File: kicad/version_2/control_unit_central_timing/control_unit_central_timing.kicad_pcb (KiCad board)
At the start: 2 copper layers, 100 x 100 mm, 25 parts

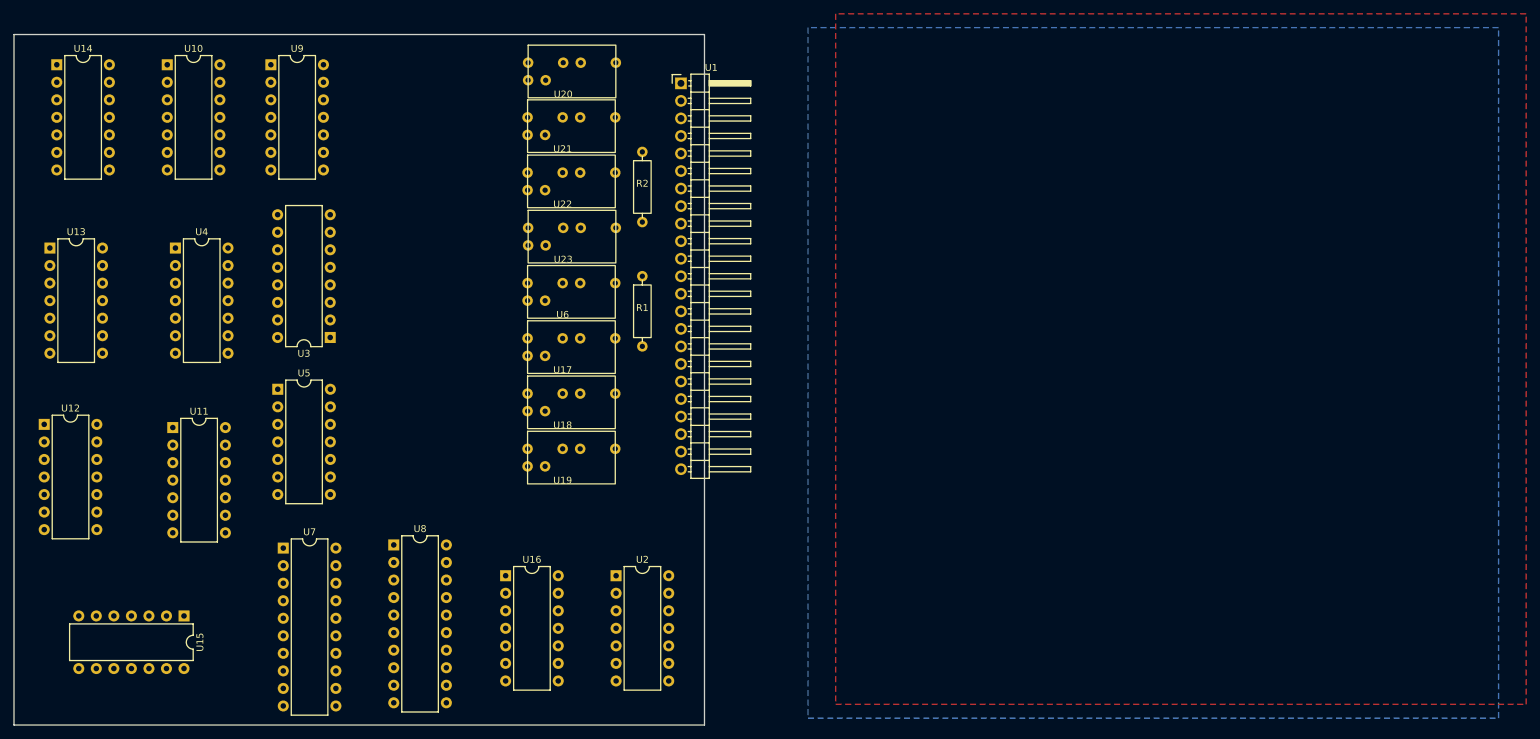
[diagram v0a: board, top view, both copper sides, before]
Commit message: Screen emulator working
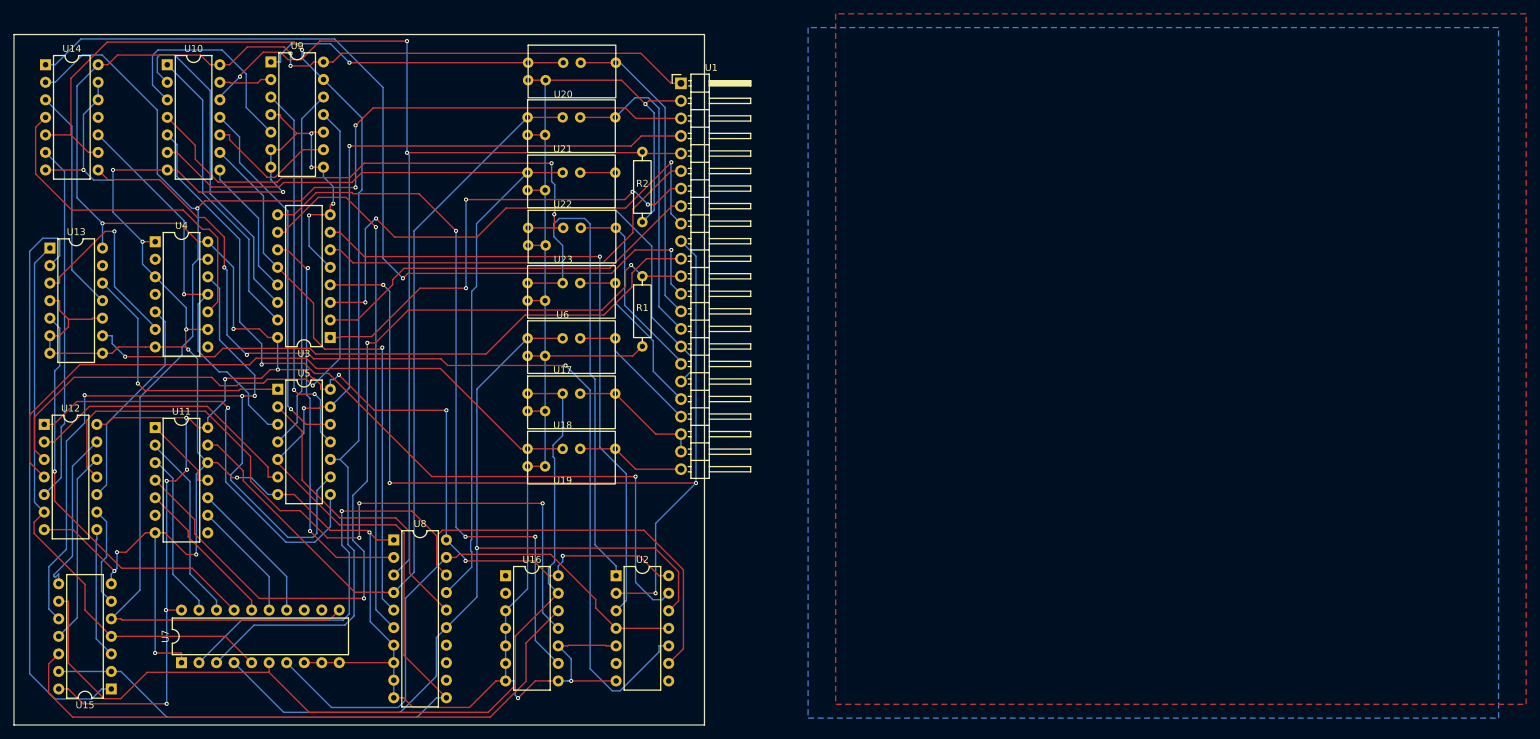
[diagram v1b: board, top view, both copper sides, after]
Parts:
- moved U7 22.2 mm to (135.3, 141.0), turned to 90 degrees
- moved U15 14.9 mm to (125.1, 144.8), turned to 180 degrees
- moved U4 3.06 mm to (131.5, 80.0)
- moved U11 2.56 mm to (131.4, 106.9)
- moved U14 1.63 mm to (115.6, 54.4)
- moved U8 0.73 mm to (166.0, 123.2)
- moved U9 0.40 mm to (148.2, 54.0)
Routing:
- net Net-(U1-GND): track 0.00 -> 539.5 mm, vias 0 -> 19
- net Net-(U1-V+): track 0.00 -> 345.2 mm, vias 0 -> 15
- net Net-(U1-A_CLK): track 0.00 -> 220.0 mm, vias 0 -> 3
- net Net-(U1-B_CLK): track 0.00 -> 209.9 mm, vias 0 -> 2
- net Net-(U14-2B): track 0.00 -> 164.8 mm, vias 0 -> 1
- net Net-(U1-BUS_MOVE_DONE): track 0.00 -> 150.1 mm, vias 0 -> 3
- net Net-(U14-4Q): track 0.00 -> 149.0 mm, vias 0 -> 3
- net Net-(U1-INSTRUCTION-3): track 0.00 -> 141.1 mm, vias 0 -> 4
- net Net-(U15-4B): track 0.00 -> 135.7 mm
- net Net-(U17-IN): track 0.00 -> 130.8 mm, vias 0 -> 1
- net Net-(U1-BUS_READ_GOTO-DECIDER): track 0.00 -> 129.7 mm, vias 0 -> 2
- net Net-(U1-START): track 0.00 -> 129.2 mm, vias 0 -> 3
- net Net-(U10-1B): track 0.00 -> 126.0 mm
- net Net-(U10-1A): track 0.00 -> 121.5 mm, vias 0 -> 2
- net Net-(U11-OB): track 0.00 -> 118.5 mm
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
